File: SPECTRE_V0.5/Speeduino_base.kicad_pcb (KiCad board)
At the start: 2 copper layers, 100 x 93 mm, 185 parts, among them J1 Conn_01x04_Male, J2 Conn_02x04_Odd_Even, J3 Conn_01x06_Male, Q1 2N7002, Q10 BSP78, Q11 BSP78, Q12 BSP78, Q13 BSP78, Q14 BSP78, Q15 BSP78, Q16 BSP78, Q17 BSP78, Q18 BSP78, Q2 CJ2302, Q3 CJ2302, Q4 CJ2302, Q5 BSP78, Q6 BSP78, Q7 CJ2302, Q8 CJ2302, Q9 CJ2302, U1 MAX9926UAEE+, U2 molex_48pin, U3 LM78M05_TO220, U4 MAX3232

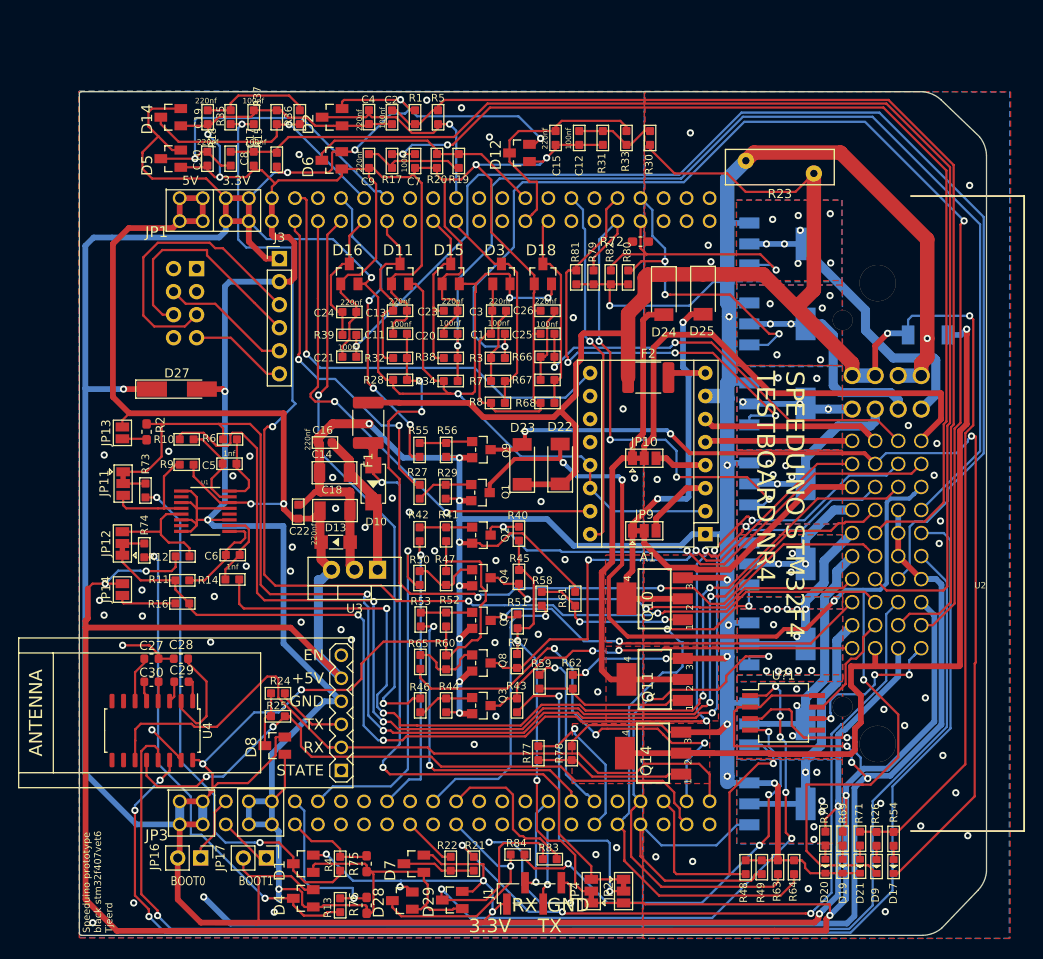
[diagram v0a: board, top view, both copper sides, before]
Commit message: update silkscreen
Updated silkscreen V0.4. Start switchable flyback diode in V0.5 for PWM control of injectors
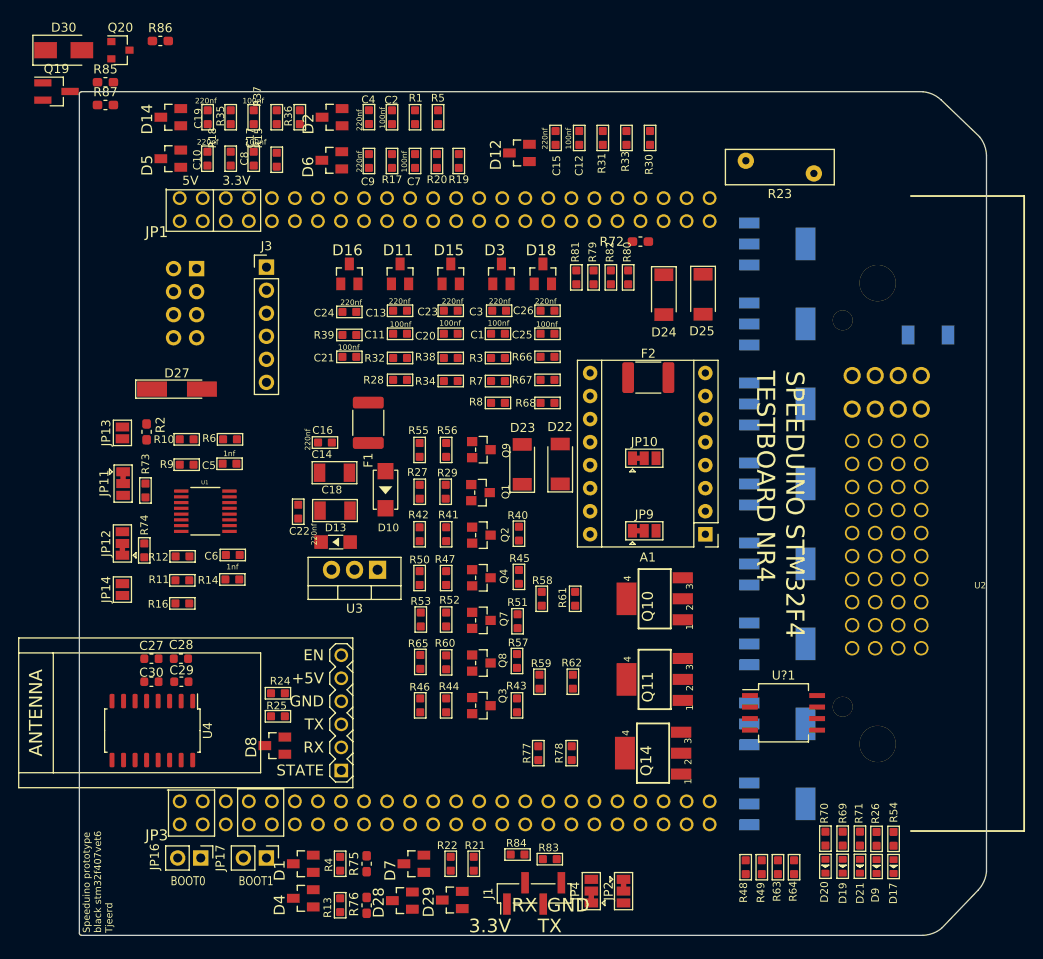
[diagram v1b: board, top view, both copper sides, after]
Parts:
- added D30: SS310, Diode_SMD:D_SMA, F.Cu at (112.3, 12.4)
- added Q19: SMD-MOSFET-N-CH-30V-5.8A-AO3400(SOT-23), Package_TO_SOT_SMD:SOT-23_Handsoldering, F.Cu at (111.5, 17.0)
- added Q20: AO3401A, Package_TO_SOT_SMD:SOT-23, F.Cu at (118.5, 12.4)
- added R85: 1K, Resistor_SMD:R_0603_1608Metric_Pad1.05x0.95mm_HandSolder, F.Cu at (116.9, 16.0)
- added R86: 1K, Resistor_SMD:R_0603_1608Metric_Pad1.05x0.95mm_HandSolder, F.Cu at (122.9, 11.4)
- added R87: 1K, Resistor_SMD:R_0603_1608Metric_Pad1.05x0.95mm_HandSolder, F.Cu at (116.9, 18.5)
- moved J3 1.71 mm to (134.6, 36.3)
- moved D10 1.50 mm to (147.8, 60.9)
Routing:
- net GND: track 576.6 -> 0.00 mm, vias 58 -> 0
- net 3.3V: track 568.1 -> 0.00 mm, vias 17 -> 0
- net 5V: track 360.3 -> 0.00 mm, vias 7 -> 0
- net PWR_GND: track 353.2 -> 0.00 mm, vias 41 -> 0
- net VBAT: track 212.8 -> 0.00 mm, vias 2 -> 0
- net RS232_TX: track 149.1 -> 0.00 mm, vias 3 -> 0
- net VR1+: track 148.9 -> 0.00 mm, vias 5 -> 0
- net RS232_RX: track 145.9 -> 0.00 mm, vias 1 -> 0
- net IAT: track 139.8 -> 0.00 mm
- net TPS: track 134.8 -> 0.00 mm, vias 1 -> 0
- net MAP: track 130.4 -> 0.00 mm, vias 4 -> 0
- net FUEL_PUMP: track 130.1 -> 0.00 mm, vias 4 -> 0
- net O2_2: track 128.9 -> 0.00 mm, vias 2 -> 0
- net VR1-: track 126.3 -> 0.00 mm, vias 4 -> 0
- net VR2+: track 124.7 -> 0.00 mm, vias 5 -> 0
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- removed copper zone on F.Cu, net BOOST-OUT
- removed copper zone on B.Cu, net GND
- removed copper zone on F.Cu, net GND
- removed copper zone on F.Cu, net IDLE1-OUT
- removed copper zone on F.Cu, net IDLE2-OUT
- removed copper zone on B.Cu, net INJ1-OUT
- removed copper zone on F.Cu, net INJ1-OUT
- removed copper zone on B.Cu, net INJ2-OUT
- removed copper zone on F.Cu, net INJ2-OUT
- removed copper zone on B.Cu, net INJ3-OUT
- removed copper zone on F.Cu, net INJ3-OUT
- removed copper zone on B.Cu, net INJ4-OUT
- removed copper zone on F.Cu, net INJ4-OUT
- removed copper zone on B.Cu, net INJ5-OUT
- removed copper zone on F.Cu, net INJ5-OUT
- removed copper zone on B.Cu, net INJ6-OUT
- removed copper zone on F.Cu, net INJ6-OUT
- removed copper zone on B.Cu, net INJ7-OUT
- removed copper zone on F.Cu, net INJ7-OUT
- removed copper zone on B.Cu, net INJ8-OUT
- removed copper zone on F.Cu, net INJ8-OUT
- removed copper zone on B.Cu, net PWR_GND
- removed copper zone on F.Cu, net PWR_GND

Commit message: Routing V0.5
Started routing board V0.5
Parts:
- added D31: SS310, Diode_SMD:D_SMA, F.Cu at (190.5, 35.4)
- added D32: SS310, Diode_SMD:D_SMA, F.Cu at (190.4, 44.7)
- added D33: SS310, Diode_SMD:D_SMA, F.Cu at (190.5, 26.4)
- added Q21: SMD-MOSFET-N-CH-30V-5.8A-AO3400(SOT-23), Package_TO_SOT_SMD:SOT-23_Handsoldering, F.Cu at (142.0, 64.8)
- added Q22: SMD-MOSFET-N-CH-30V-5.8A-AO3400(SOT-23), Package_TO_SOT_SMD:SOT-23_Handsoldering, F.Cu at (142.1, 59.9)
- added Q23: AO3401A, Package_TO_SOT_SMD:SOT-23_Handsoldering, B.Cu at (194.3, 44.8)
- added Q24: AO3401A, Package_TO_SOT_SMD:SOT-23_Handsoldering, B.Cu at (194.4, 26.5)
- added Q25: BSP78, Speeduino_base:SOT223, B.Cu at (191.2, 49.4)
- added Q26: BSP78, Speeduino_base:SOT223, B.Cu at (191.2, 30.9)
- added R88: 10k, Speeduino_base:R_0603_1608Metric_Pad1.05x0.95mm_HandSolder, F.Cu at (179.4, 34.7)
- added R89: 1K, Speeduino_base:R_0603_1608Metric_Pad1.05x0.95mm_HandSolder, F.Cu at (138.4, 64.7)
- added R90: 1K, Speeduino_base:R_0603_1608Metric_Pad1.05x0.95mm_HandSolder, F.Cu at (138.2, 59.9)
- added R91: 1K, Speeduino_base:R_0603_1608Metric_Pad1.05x0.95mm_HandSolder, F.Cu at (147.8, 64.8)
- added R92: 1K, Speeduino_base:R_0603_1608Metric_Pad1.05x0.95mm_HandSolder, F.Cu at (145.6, 64.8)
- added R93: 1K, Speeduino_base:R_0603_1608Metric_Pad1.05x0.95mm_HandSolder, F.Cu at (147.8, 60.0)
- added R94: 1K, Speeduino_base:R_0603_1608Metric_Pad1.05x0.95mm_HandSolder, F.Cu at (145.6, 60.0)
- added R95: 10k, Speeduino_base:R_0603_1608Metric_Pad1.05x0.95mm_HandSolder, F.Cu at (177.0, 34.7)
- added R96: 10k, Speeduino_base:R_0603_1608Metric_Pad1.05x0.95mm_HandSolder, F.Cu at (181.6, 34.7)
- D26: moved to F.Cu
- Q16: value BSP78 -> SMD-MOSFET-N-CH-30V-5.8A-AO3400(SOT-23); footprint Speeduino_base:SOT223 -> Package_TO_SOT_SMD:SOT-23_Handsoldering; moved to F.Cu
- Q17: value BSP78 -> AO3401A; footprint Speeduino_base:SOT223 -> Package_TO_SOT_SMD:SOT-23_Handsoldering
- Q20: footprint Package_TO_SOT_SMD:SOT-23 -> Package_TO_SOT_SMD:SOT-23_Handsoldering; moved to B.Cu
- R79: footprint Speeduino_base:R0603 -> Speeduino_base:R_0603_1608Metric_Pad1.05x0.95mm_HandSolder
- R80, R81, R82: value 10k -> 1K; footprint Speeduino_base:R0603 -> Speeduino_base:R_0603_1608Metric_Pad1.05x0.95mm_HandSolder
- R85, R86, R87: footprint Resistor_SMD:R_0603_1608Metric_Pad1.05x0.95mm_HandSolder -> Speeduino_base:R_0603_1608Metric_Pad1.05x0.95mm_HandSolder
- moved D30 88.6 mm to (190.6, 53.8)
- moved Q20 86.5 mm to (194.4, 53.8), turned to 180 degrees
- moved R86 63.0 mm to (147.8, 69.2), turned to 270 degrees
- moved Q19 60.6 mm to (142.0, 69.3)
- moved D26 59.1 mm to (173.4, 92.0)
- moved R87 58.3 mm to (145.5, 69.2), turned to 90 degrees
- moved R85 57.5 mm to (138.4, 69.3), turned to 90 degrees
- moved Q16 50.5 mm to (142.1, 55.1), turned to 0 degrees
- moved D24 44.9 mm to (173.4, 84.0), turned to 0 degrees
- moved R80 40.2 mm to (138.3, 55.1), turned to 90 degrees
- moved D25 37.6 mm to (173.3, 75.8), turned to 0 degrees
- moved R82 32.3 mm to (145.6, 55.2), turned to 90 degrees
- moved R81 27.6 mm to (147.7, 55.2), turned to 270 degrees
- moved C16 24.7 mm to (116.5, 53.3), turned to 180 degrees
- moved U3 22.7 mm to (129.9, 54.6), turned to 270 degrees
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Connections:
- D30 pad 1: VBAT_F1 -> V_IDLE
- JP4 pad 3: VBAT_F1 -> Net-(JP4-Pad3)
- Q15 pad 1: PE12 -> PE9
- Q16 pad 1: PE13 -> PE10
- Q16 pad 2: INJ7-OUT -> PWR_GND
- Q16 pad 3: PWR_GND -> Net-(Q16-Pad3)
- Q17 pad 1: PE11 -> Net-(Q17-Pad1)
- Q17 pad 2: INJ6-OUT -> INJ7-OUT
- Q17 pad 3: PWR_GND -> Net-(D31-Pad2)
- Q18 pad 1: PE14 -> PE13
- Q18 pad 2: INJ8-OUT -> INJ7-OUT
- Q18 pad 4: INJ8-OUT -> INJ7-OUT
- Q19 pad 1: Net-(Q19-Pad1) -> PE8
- R79 pad 1: PE12 -> PE9
- R80 pad 1: PE13 -> 3.3V
- R80 pad 2: PWR_GND -> PE10
- R81 pad 1: PE11 -> Net-(D31-Pad2)
- R81 pad 2: PWR_GND -> Net-(Q17-Pad1)
- R82 pad 1: PE14 -> Net-(Q17-Pad1)
- R82 pad 2: PWR_GND -> Net-(Q16-Pad3)
- R85 pad 2: Net-(Q19-Pad1) -> PE8
- U2 pad 14: VR1+ -> O2_2
- U2 pad 17: FUEL_PUMP -> IAT
- U2 pad 18: VR2- -> IAT_2
- U2 pad 19: VR2+ -> FUEL_PUMP
- U2 pad 21: CLT_2 -> RS232_TX
- U2 pad 23: VR1- -> O2
- U2 pad 25: RS232_TX -> MAP
- U2 pad 27: O2 -> CLT_2
- U2 pad 29: RS232_RX -> CANH
- U2 pad 34: TPS -> RS232_RX
- U2 pad 35: IAT -> TPS
- U2 pad 39: MAP -> VR2-
- U2 pad 41: O2_2 -> VR2+
- U2 pad 42: IAT_2 -> VR1-
- U2 pad 43: CANH -> VR1+
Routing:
- net VR2-: track 0.00 -> 186.3 mm
- net RS232_TX: track 0.00 -> 176.8 mm, vias 0 -> 1
- net GND: track 0.00 -> 170.7 mm, vias 0 -> 1
- net PWR_GND: track 0.00 -> 164.6 mm, vias 0 -> 3
- net RS232_RX: track 0.00 -> 163.1 mm
- net VR1-: track 0.00 -> 145.0 mm
- net 5V: track 0.00 -> 136.9 mm
- net VR2+: track 0.00 -> 130.9 mm
- net MAP: track 0.00 -> 129.6 mm, vias 0 -> 1
- net IAT: track 0.00 -> 121.5 mm, vias 0 -> 1
- net FUEL_PUMP: track 0.00 -> 91.6 mm, vias 0 -> 2
- net FAN: track 0.00 -> 88.8 mm, vias 0 -> 2
- net TPS: track 0.00 -> 88.7 mm, vias 0 -> 2
- net O2: track 0.00 -> 88.0 mm, vias 0 -> 2
- net FLEX_FUEL_IN: track 0.00 -> 84.7 mm, vias 0 -> 1
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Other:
- board text added: "SPEEDUINO STM32F4 TESTBOARD NR5"
- board text removed: "SPEEDUINO STM32F4 TESTBOARD NR4"

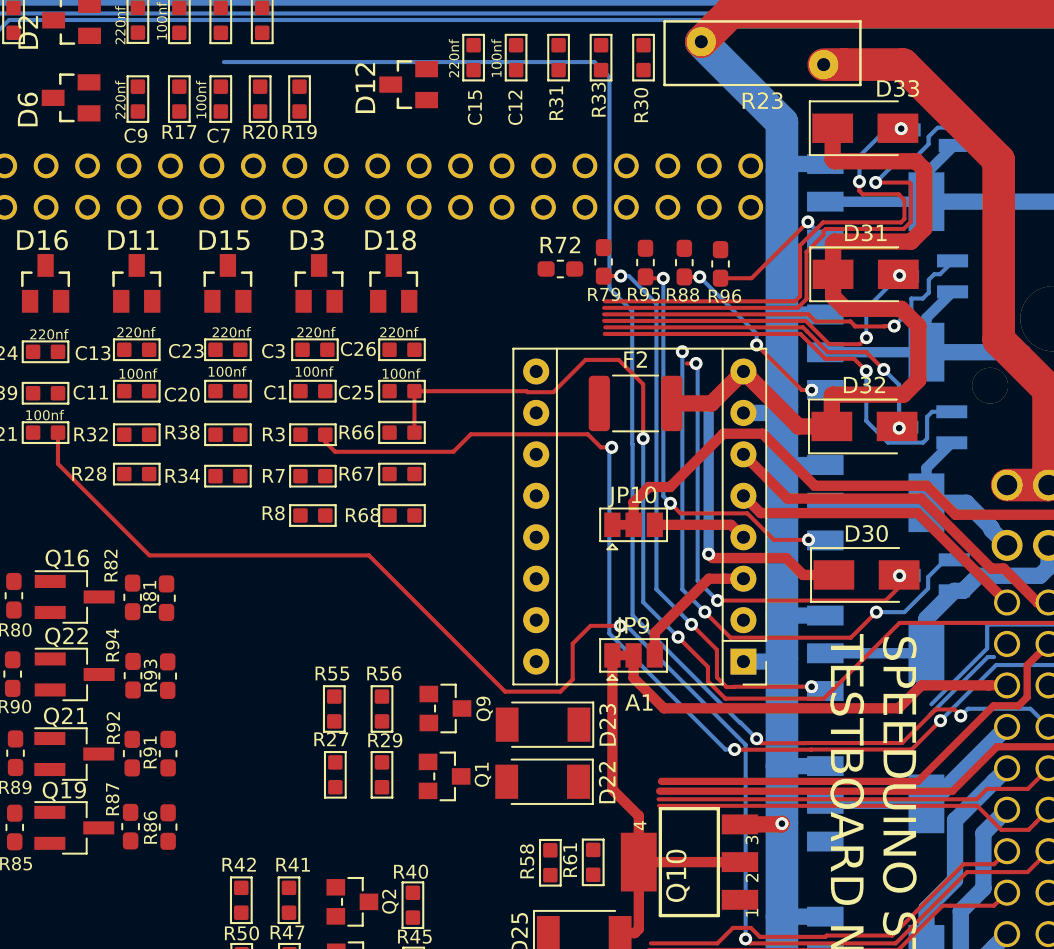
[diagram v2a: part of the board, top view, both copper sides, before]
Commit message: peak & hold injector driver update
Updates to Low-z PWM peak & hold injector driver schematic.
Updates simulation low-z driver.
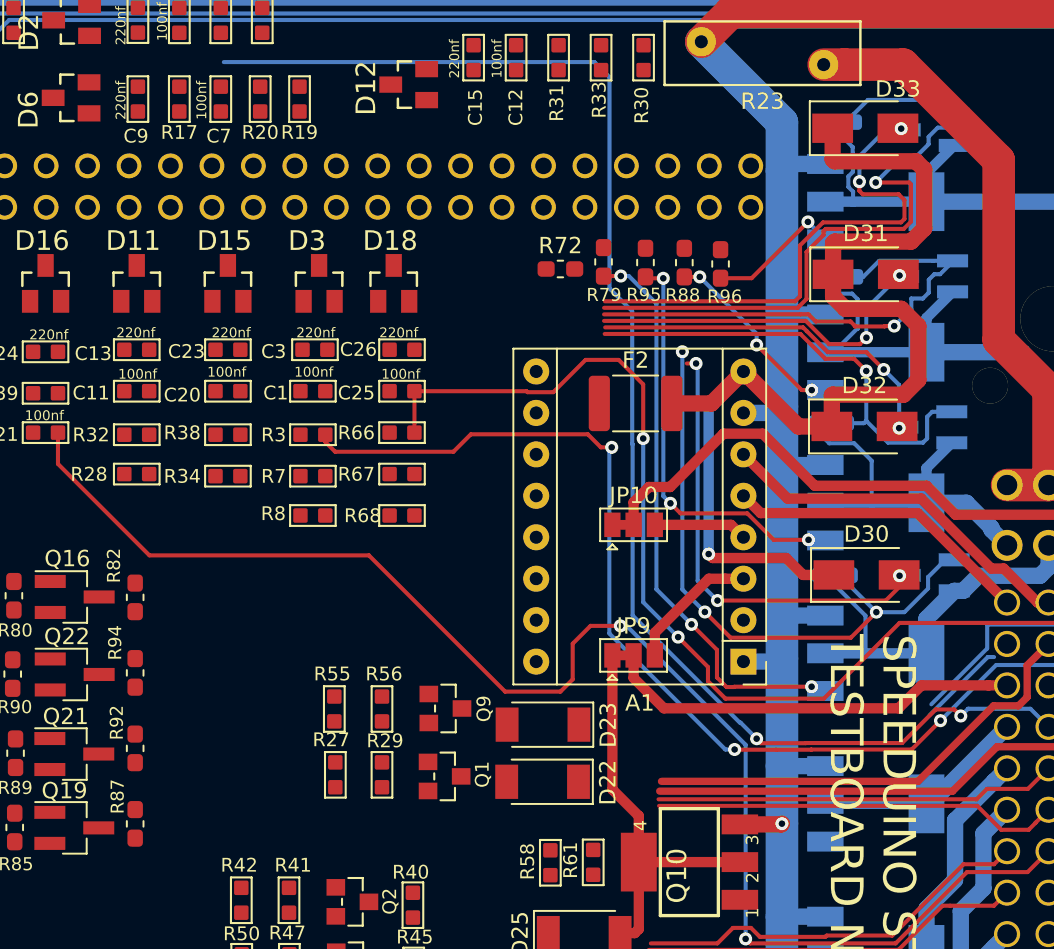
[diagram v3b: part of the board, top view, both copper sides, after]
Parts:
- Q16, Q19, Q21, Q22: value SMD-MOSFET-N-CH-30V-5.8A-AO3400(SOT-23) -> SMD-MOSFET-N-CH-55V-2.1A-AO3422(SOT-23)
- R81, R86, R91, R93: value 1K -> 470; moved to B.Cu
- R82, R87, R92, R94: value 1K -> 1K8
- moved R93 53.3 mm to (188.9, 26.1), turned to 180 degrees
- moved R81 45.8 mm to (189.0, 35.5), turned to 180 degrees
- moved R91 45.4 mm to (188.4, 44.5), turned to 180 degrees
- moved R86 43.7 mm to (188.6, 53.8), turned to 180 degrees
- moved R92 0.37 mm to (145.8, 64.4)
- moved R87 0.33 mm to (145.8, 69.1)
- moved R94 0.22 mm to (145.8, 59.8)
- moved R82 0.16 mm to (145.8, 55.2)
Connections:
- R81 pad 1: Net-(D31-Pad2) -> Net-(Q17-Pad1)
- R81 pad 2: Net-(Q17-Pad1) -> INJ7-OUT
- R86 pad 1: Net-(D30-Pad2) -> Net-(Q20-Pad1)
- R86 pad 2: Net-(Q20-Pad1) -> INJ5-OUT
- R91 pad 1: Net-(D32-Pad2) -> Net-(Q23-Pad1)
- R91 pad 2: Net-(Q23-Pad1) -> INJ6-OUT
- R93 pad 1: Net-(D33-Pad2) -> Net-(Q24-Pad1)
- R93 pad 2: Net-(Q24-Pad1) -> INJ8-OUT
- U2 pad 13: IGN1-OUT -> IGN4-OUT
- U2 pad 16: IGN4-OUT -> IGN1-OUT
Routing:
- net Net-(Q24-Pad1): track 34.5 -> 42.3 mm
- net INJ7-OUT: track 36.8 -> 44.0 mm
- net INJ6-OUT: track 16.6 -> 23.8 mm
- net Net-(Q17-Pad1): track 24.2 -> 30.6 mm
- net INJ8-OUT: track 47.0 -> 53.4 mm
- net INJ5-OUT: track 18.4 -> 24.5 mm
- net Net-(Q20-Pad1): track 34.8 -> 37.8 mm
- net Net-(Q23-Pad1): track 27.4 -> 28.7 mm
